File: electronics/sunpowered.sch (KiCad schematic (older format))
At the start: 20 parts, among them IC1 ACS713, P1 CONN_01X02, P2 CONN_02X04, P3 CONN_01X02, Q1 PSMN0R9-30YLD, T1 12A

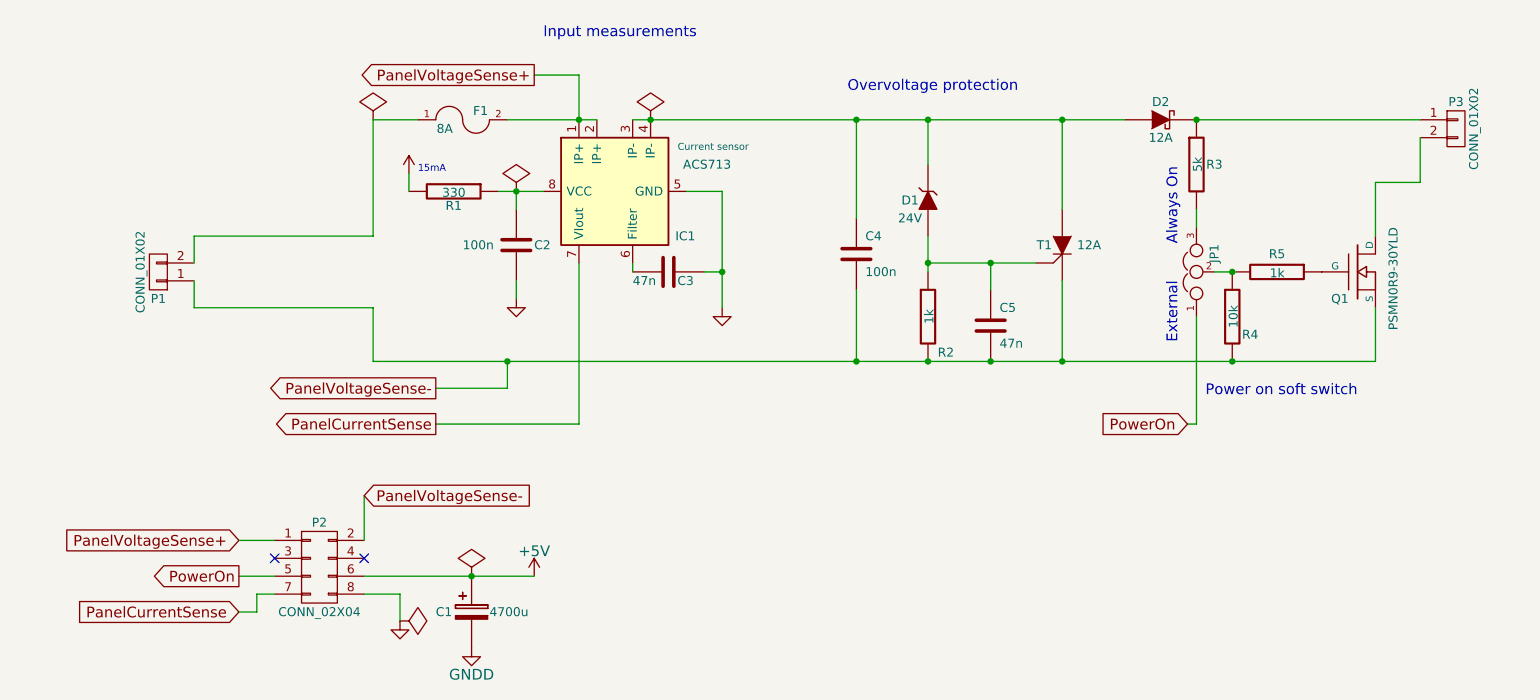
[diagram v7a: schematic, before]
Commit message: custom footprints for semiconductors, initial auto placement on the board
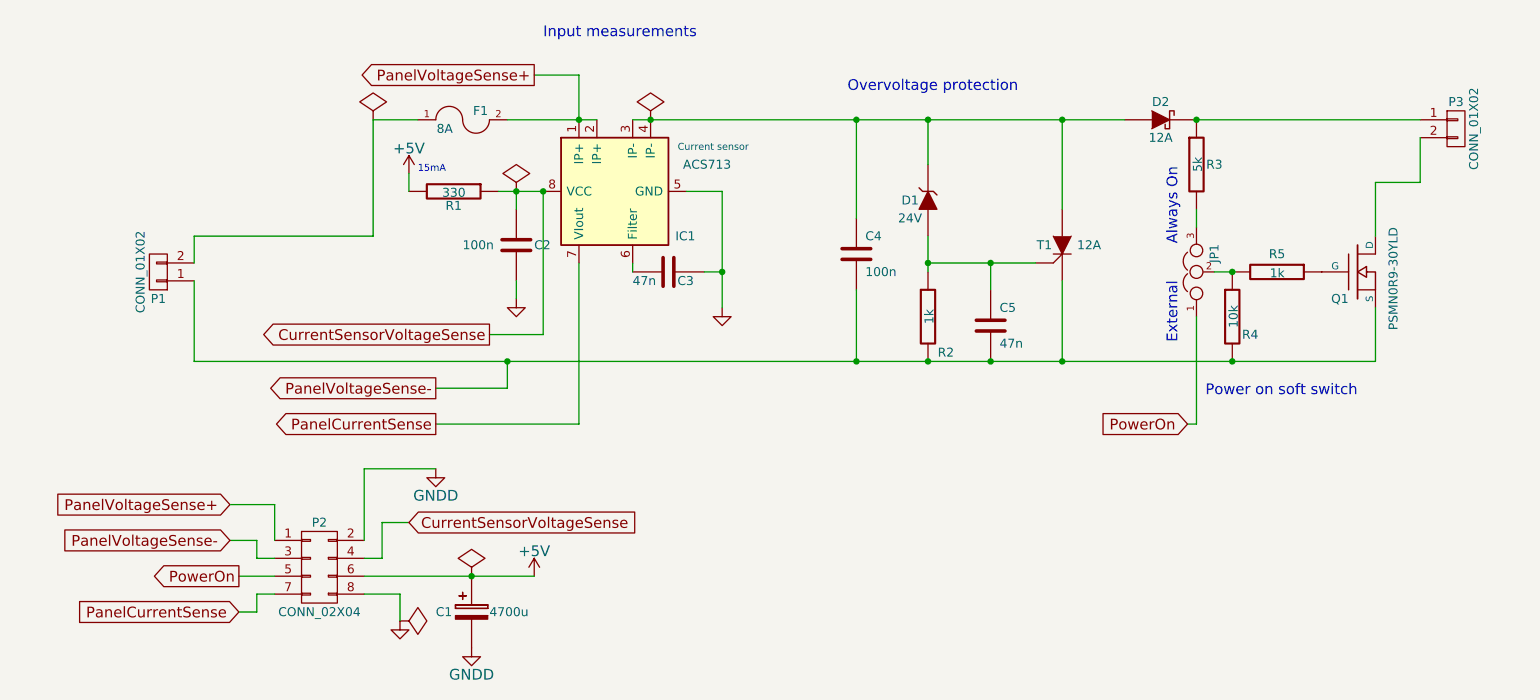
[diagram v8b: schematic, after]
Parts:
- T1: footprint Transistors_SMD:sot428 -> cyplo's:sot428
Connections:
- net GNDD: now also P2.2 (P2)
- net PanelVoltageSense-: now also P2.3 (P3); no longer P2.2 (P2)
- net CurrentSensorVoltageSense: now reaches C2.1, IC1.8 (VCC), R1.1
- net CurrentSensorVoltageSense: now also P2.4 (P4)
- no-connect marks 2 -> 0
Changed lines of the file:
@@
 F 0 "T1" V 7650 2350 50  0000 C CNN
 F 1 "12A" V 7650 2100 50  0000 C CNN
-F 2 "Transistors_SMD:sot428" H 7650 2250 60  0001 C CNN
+F 2 "cyplo's:sot428" H 7650 2250 60  0001 C CNN
 F 3 "http://www.nxp.com/documents/data_sheet/BT151S_SER_L_R.pdf" H 7650 2250 60  0001 C CNN
 	1    7650 2250
@@
 Text GLabel 3050 4100 0    60   Output ~ 0
 PowerOn
-Text GLabel 3750 3650 2    60   Input ~ 0
+Text GLabel 3000 3900 0    60   Input ~ 0
 PanelVoltageSense-
-Text GLabel 3050 3900 0    60   Input ~ 0
+Text GLabel 3000 3700 0    60   Input ~ 0
 PanelVoltageSense+
 $Comp
@@
 	1    0    0    -1
 $EndComp
-NoConn ~ 3750 4000
-NoConn ~ 3250 4000
 $Comp
 L PWR_FLAG #FLG04
@@
 P 4000 1850
 F 0 "#PWR07" H 4000 1700 60  0001 C CNN
-F 1 "+5V" H 4000 1990 60  0001 C CNN
+F 1 "+5V" H 4000 1990 60  0000 C CNN
 F 2 "" H 4000 1850 60  0000 C CNN
 F 3 "" H 4000 1850 60  0000 C CNN
@@
 Wire Wire Line
 	3800 1550 4050 1550
-Wire Wire Line
-	3800 2600 3800 2900
 Wire Wire Line
 	4950 1300 4950 1550
@@
 	2800 2200 2800 2350
 Wire Wire Line
-	2800 2450 2800 2600
+	2800 2450 2800 2900
 Wire Wire Line
 	8400 1550 9650 1550
@@
 	4550 3050 4150 3050
 Wire Wire Line
-	3800 2900 9400 2900
+	2800 2900 9400 2900
 Wire Wire Line
 	8400 2050 8400 2150
@@
 	5750 2400 5650 2400
 Connection ~ 5750 2400
-Wire Wire Line
-	3250 3900 3050 3900
-Wire Wire Line
-	3750 3650 3750 3900
 Wire Wire Line
 	3050 4100 3250 4100
@@
 	3800 2200 2800 2200
 Wire Wire Line
-	2800 2600 3800 2600
+	4750 1950 4750 2750
+Wire Wire Line
+	4750 2750 4450 2750
+Text GLabel 4450 2750 0    60   Output ~ 0
+CurrentSensorVoltageSense
+Text GLabel 4000 3800 2    60   Input ~ 0
+CurrentSensorVoltageSense
+Wire Wire Line
+	3850 3800 3850 4000
+Wire Wire Line
+	3850 4000 3750 4000
+Wire Wire Line
+	3850 3800 4000 3800
+Wire Wire Line
+	3750 3500 3750 3900
+$Comp
+L GNDD #PWR012
+U 1 1 55DCC714
+P 4150 3500
+F 0 "#PWR012" H 4150 3250 60  0001 C CNN
+F 1 "GNDD" H 4150 3350 60  0000 C CNN
+F 2 "" H 4150 3500 60  0000 C CNN
+F 3 "" H 4150 3500 60  0000 C CNN
+	1    4150 3500
+	1    0    0    -1
+$EndComp
+Wire Wire Line
+	4150 3500 3750 3500
+Wire Wire Line
+	3000 3900 3150 3900
+Wire Wire Line
+	3250 3900 3250 3700
+Wire Wire Line
+	3250 3700 3000 3700
+Wire Wire Line
+	3150 3900 3150 4000
+Wire Wire Line
+	3150 4000 3250 4000
+Connection ~ 4750 1950
 $EndSCHEMATC
